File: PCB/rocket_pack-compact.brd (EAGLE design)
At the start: 27.6 x 76.2 mm, 22 parts, among them Q2 QUARZ5, U1 TPS73632_DBV_5, U2 LTC1540, U3 MSP430FR5739_DA_38

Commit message: firmware + PCB update
Start of main firmware..mainly UART code
Update to PCB to move "command" line from radio pin 6 to 16.  Pin 6
enters command mode on boot, pin 16 enables binary command mode
(allowing the serial +++ handshake to be bypassed
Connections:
- net CONFIG_RADIO: now also U$1.P16; no longer U$1.P6
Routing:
- net CONFIG_RADIO: track 53.5 -> 40.5 mm
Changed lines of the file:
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@@
 <layers>
 <layer number="1" name="Top" color="4" fill="1" visible="yes" active="yes"/>
-<layer number="16" name="Bottom" color="1" fill="1" visible="no" active="yes"/>
+<layer number="16" name="Bottom" color="1" fill="1" visible="yes" active="yes"/>
 <layer number="17" name="Pads" color="2" fill="1" visible="yes" active="yes"/>
 <layer number="18" name="Vias" color="2" fill="1" visible="yes" active="yes"/>
@@
 </signal>
 <signal name="CONFIG_RADIO">
-<contactref element="U$1" pad="P6"/>
 <contactref element="U3" pad="28"/>
 <via x="25.758125" y="35.434375" extent="1-16" drill="0.6" shape="octagon"/>
@@
 <wire x1="25.758125" y1="36.553125" x2="27.305" y2="38.1" width="0.254" layer="16"/>
 <wire x1="25.4" y1="48.5775" x2="25.4" y2="60.96" width="0.254" layer="16"/>
-<wire x1="25.4" y1="60.96" x2="26.035" y2="61.595" width="0.254" layer="16"/>
-<via x="26.035" y="61.595" extent="1-16" drill="0.6" shape="octagon"/>
-<wire x1="26.035" y1="61.595" x2="24.13" y2="63.5" width="0.254" layer="1"/>
-<wire x1="24.13" y1="63.5" x2="7.500009375" y2="63.5" width="0.254" layer="1"/>
-<wire x1="7.500009375" y1="63.5" x2="7" y2="62.999990625" width="0.254" layer="1"/>
+<wire x1="25.4" y1="60.96" x2="26.914475" y2="62.474475" width="0.254" layer="16"/>
 <wire x1="27.305" y1="46.6725" x2="25.4" y2="48.5775" width="0.254" layer="16"/>
+<contactref element="U$1" pad="P16"/>
+<wire x1="28.470225" y1="65.497075" x2="26.7589" y2="65.497075" width="0.254" layer="1"/>
+<via x="26.7589" y="65.497075" extent="1-16" drill="0.6" shape="octagon"/>
+<wire x1="26.7589" y1="65.497075" x2="26.44775" y2="65.185925" width="0.254" layer="16"/>
+<wire x1="26.44775" y1="65.185925" x2="26.44775" y2="64.0969" width="0.254" layer="16"/>
+<wire x1="26.44775" y1="64.0969" x2="26.914475" y2="63.630175" width="0.254" layer="16"/>
+<wire x1="26.914475" y1="63.630175" x2="26.914475" y2="62.474475" width="0.254" layer="16"/>
+<wire x1="28.470225" y1="65.497075" x2="28.781375" y2="65.218615625" width="0.254" layer="1"/>
+<wire x1="28.781375" y1="65.218615625" x2="29" y2="64.999990625" width="0.254" layer="1"/>
 </signal>
 <signal name="SLEEP_RADIO">

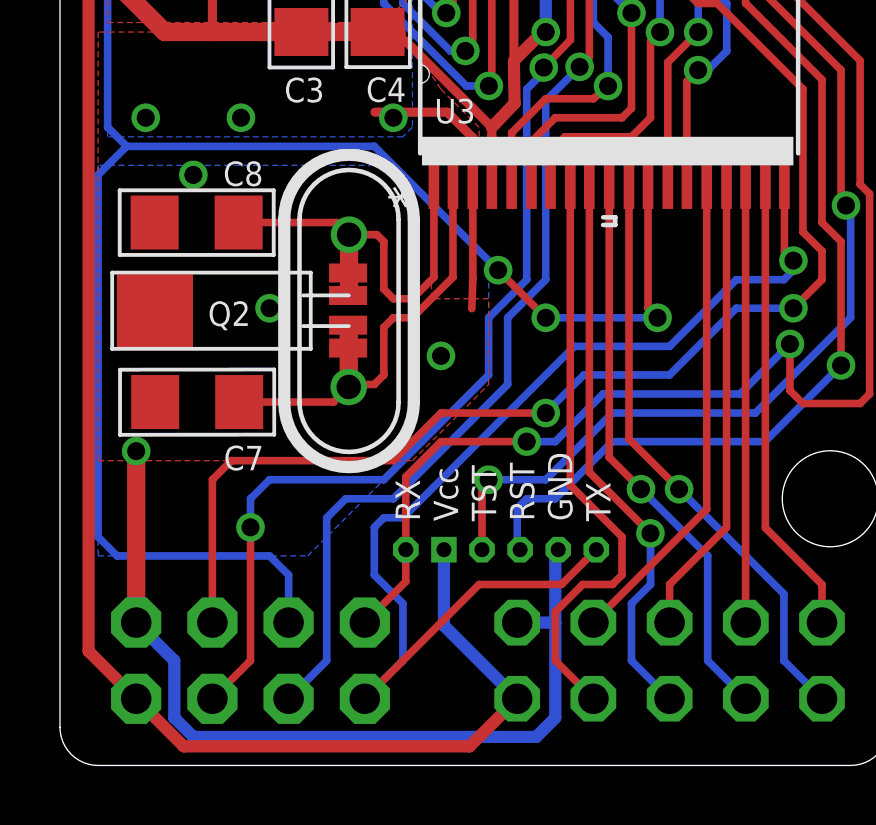
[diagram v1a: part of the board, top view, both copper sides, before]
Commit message: Added sensor state machine
Sensor state machine added with startup/shutdown handshaking sequence
with base station as well as heartbeat.

Issue with incoming (from base station) commands being blocked when
radio is burst transmitting data.
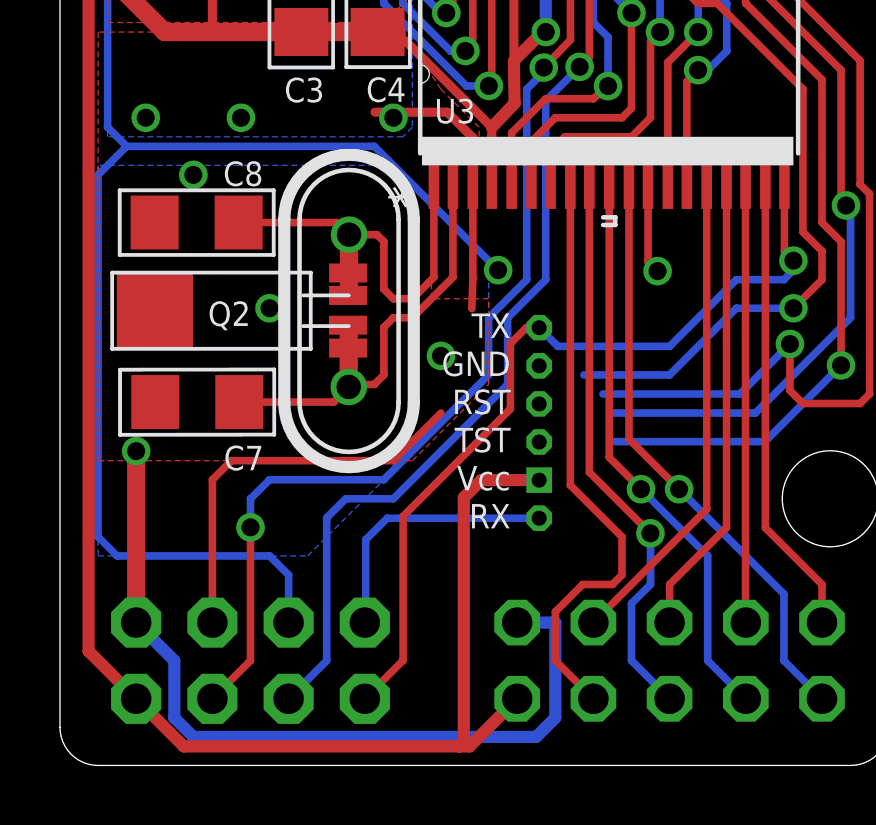
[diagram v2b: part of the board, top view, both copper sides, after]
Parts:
- moved U$2 4.90 mm to (19.8, 16.8), turned to 180 degrees
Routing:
- net TX_DB: track 36.9 -> 27.8 mm
- net STE_DB: track 57.2 -> 49.7 mm, vias 3 -> 2
- net TEST: track 29.7 -> 22.2 mm, vias 2 -> 1
- net RST: track 41.6 -> 36.0 mm
- net CLK_DB: track 40.6 -> 35.3 mm, vias 2 -> 1
- net +3V3: track 169.2 -> 174.4 mm
- net RX_DB: track 40.1 -> 35.8 mm, vias 2 -> 1
- net GND: track 77.5 -> 75.1 mm

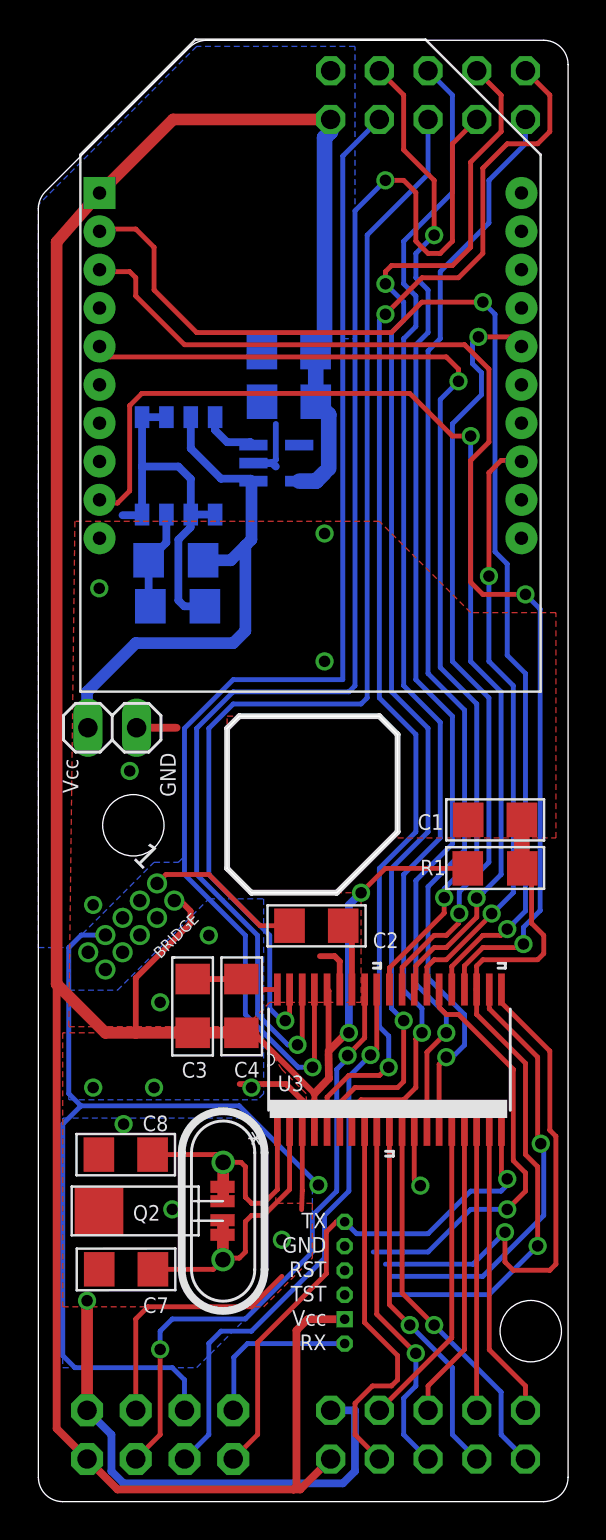
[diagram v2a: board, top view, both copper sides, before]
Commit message: Version 0.2
Moved programming header to no longer interfere with headers
Fixed pinout on radio module to allow binary programming
Added power indicator LED
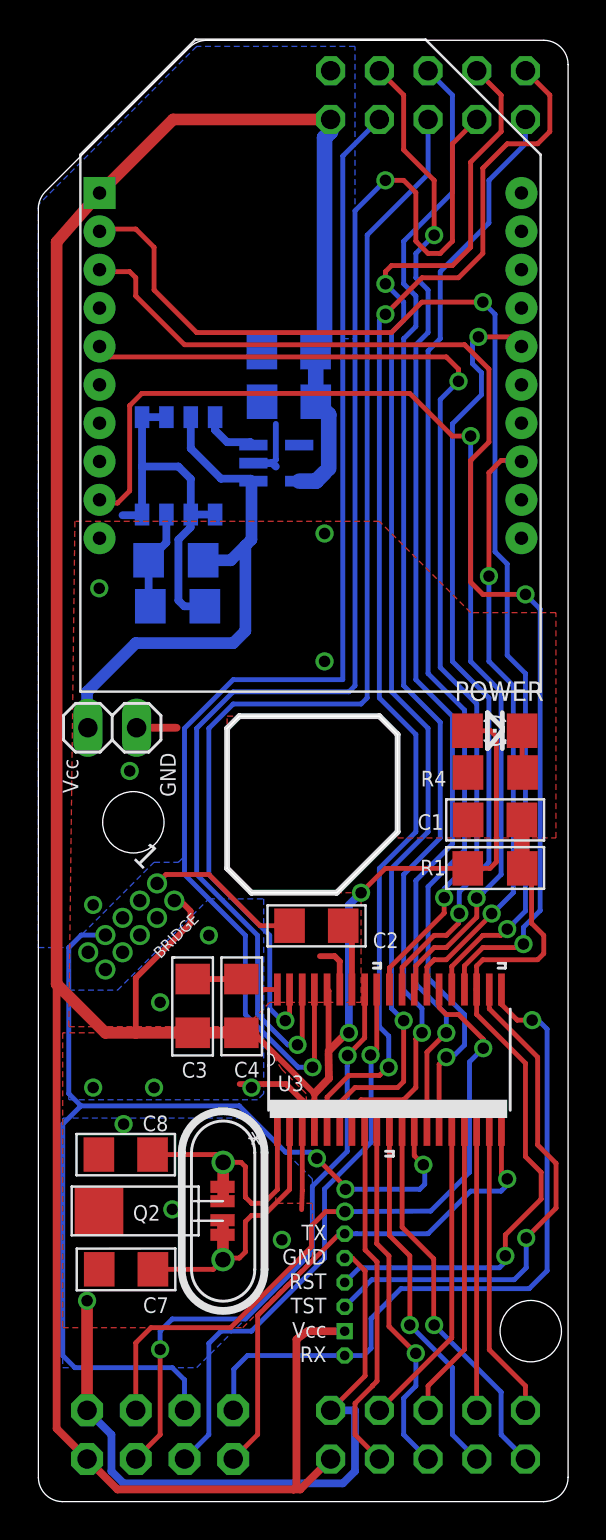
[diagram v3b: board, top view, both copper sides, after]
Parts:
- added LED1: 2V, adafruit:1206
- added R4: 100, adafruit:R1206
- C7, C8: value 12p -> 23p
- R2: value 5.1M -> 2M
- R3: value 3M -> 1.18M
- moved U$2 0.62 mm to (19.8, 16.2)
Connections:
- new net LED: LED1.C, R4.2
- net +3V3: now also LED1.A
- net GND: now also R4.1
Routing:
- net GND: track 75.1 -> 84.4 mm
- net +3V3: track 174.4 -> 183.6 mm
- net STE_DB: track 49.7 -> 55.6 mm, vias 2 -> 3
- net TEST: track 22.2 -> 26.9 mm
- net LED: track 0.00 -> 2.86 mm
- net RX_DB: track 35.8 -> 37.8 mm
- net RST: track 36.0 -> 37.9 mm
- net P3.0: track 19.9 -> 18.4 mm
- net CLK_DB: track 35.3 -> 36.4 mm, vias 1 -> 2
- net TX_DB: track 27.8 -> 26.8 mm
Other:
- board text added: "POWER"
- board text added: "Rocket Pack V0.2"
- board text removed: "Rocket Pack V0.1"
